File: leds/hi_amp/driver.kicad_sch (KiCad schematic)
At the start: 6 parts, among them U4 TPS73733DCQ_C5220270

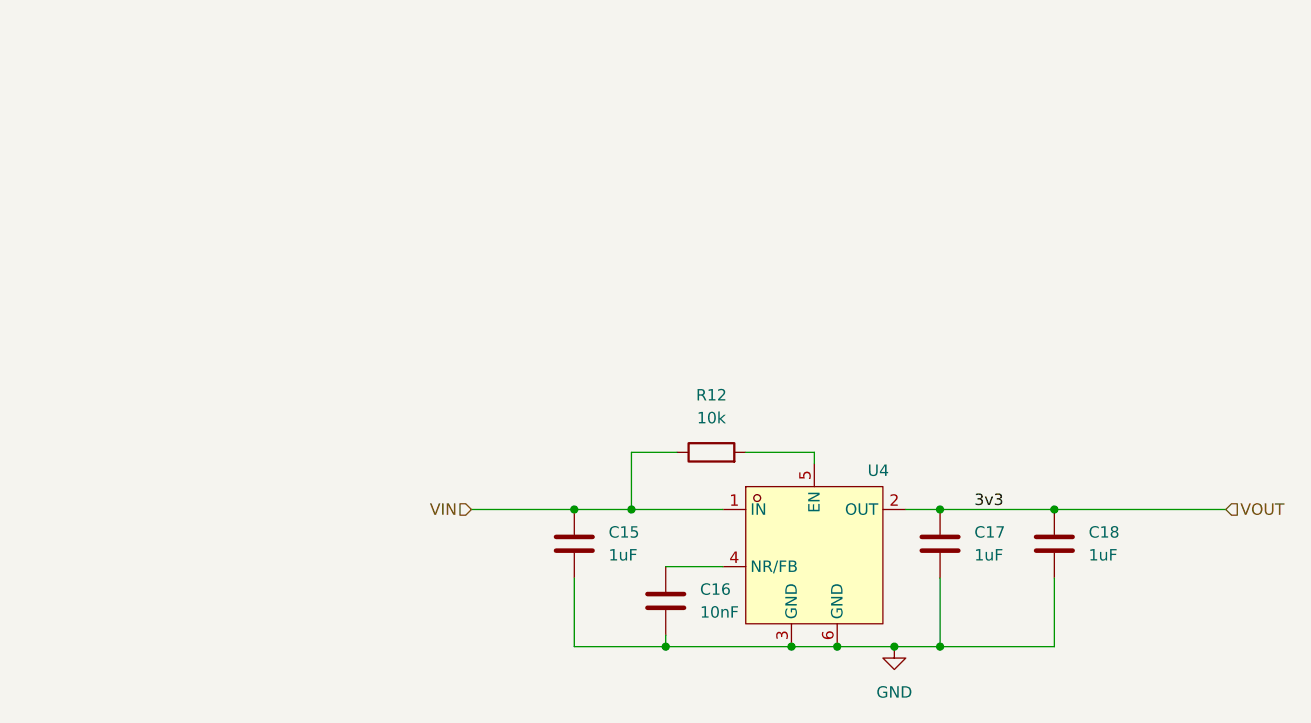
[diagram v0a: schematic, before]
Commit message: add stronger gate driver to LEDs
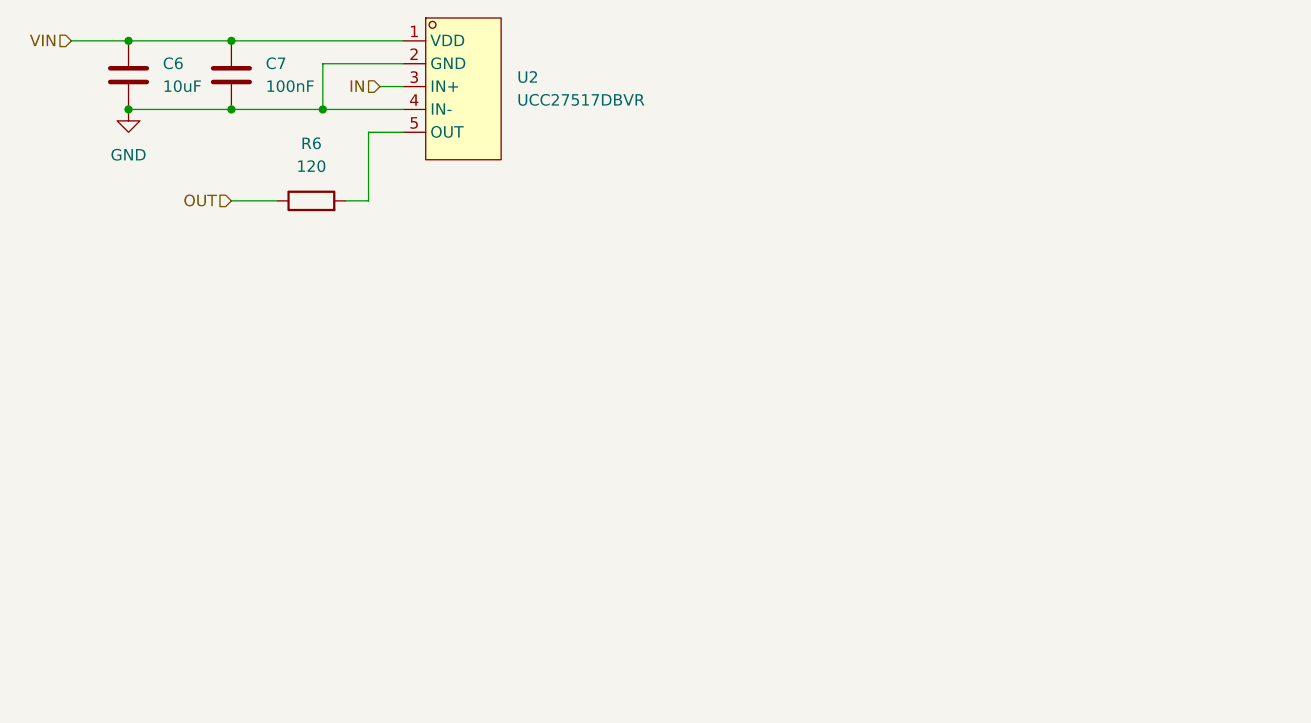
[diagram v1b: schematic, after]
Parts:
- removed C15, C17, C18: 1uF, Capacitor_SMD:C_0603_1608Metric, symbol Device:C
- removed C16: 10nF, Capacitor_SMD:C_0603_1608Metric, symbol Device:C
- removed R12: 10k, Resistor_SMD:R_0603_1608Metric, symbol Device:R
- removed U4: TPS73733DCQ_C5220270, easyeda2kicad:SOT-223-6_L6.5-W3.5-P1.27-LS7.0-BR, symbol easyeda2kicad:TPS73733DCQ_C5220270
- added C6: 10uF, Capacitor_SMD:C_0603_1608Metric, symbol Device:C
- added C7: 100nF, Capacitor_SMD:C_0603_1608Metric, symbol Device:C
- added R6: 120, Resistor_SMD:R_0805_2012Metric_Pad1.20x1.40mm_HandSolder, symbol Device:R
- added U2: UCC27517DBVR, easyeda2kicad:SOT-23-5_L3.0-W1.7-P0.95-LS2.8-BR, symbol easyeda2kicad:UCC27517DBVR
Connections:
- net GND: now also C6.2, C7.2, U2.2 (GND), U2.4 (IN-)
- net VIN: now also C6.1, C7.1, U2.1 (VDD)
- new net: R6.2, U2.5 (OUT)
- new net IN: U2.3 (IN+)
- new net OUT: R6.1
